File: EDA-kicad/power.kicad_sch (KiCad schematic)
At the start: 86 parts, among them Q4 NMOS, SW6 CHP-041B, U10 BAT-CONNECTOR-FLTS22WR00, U11 BQ25792RQMR, U2 TPS650250RHBR

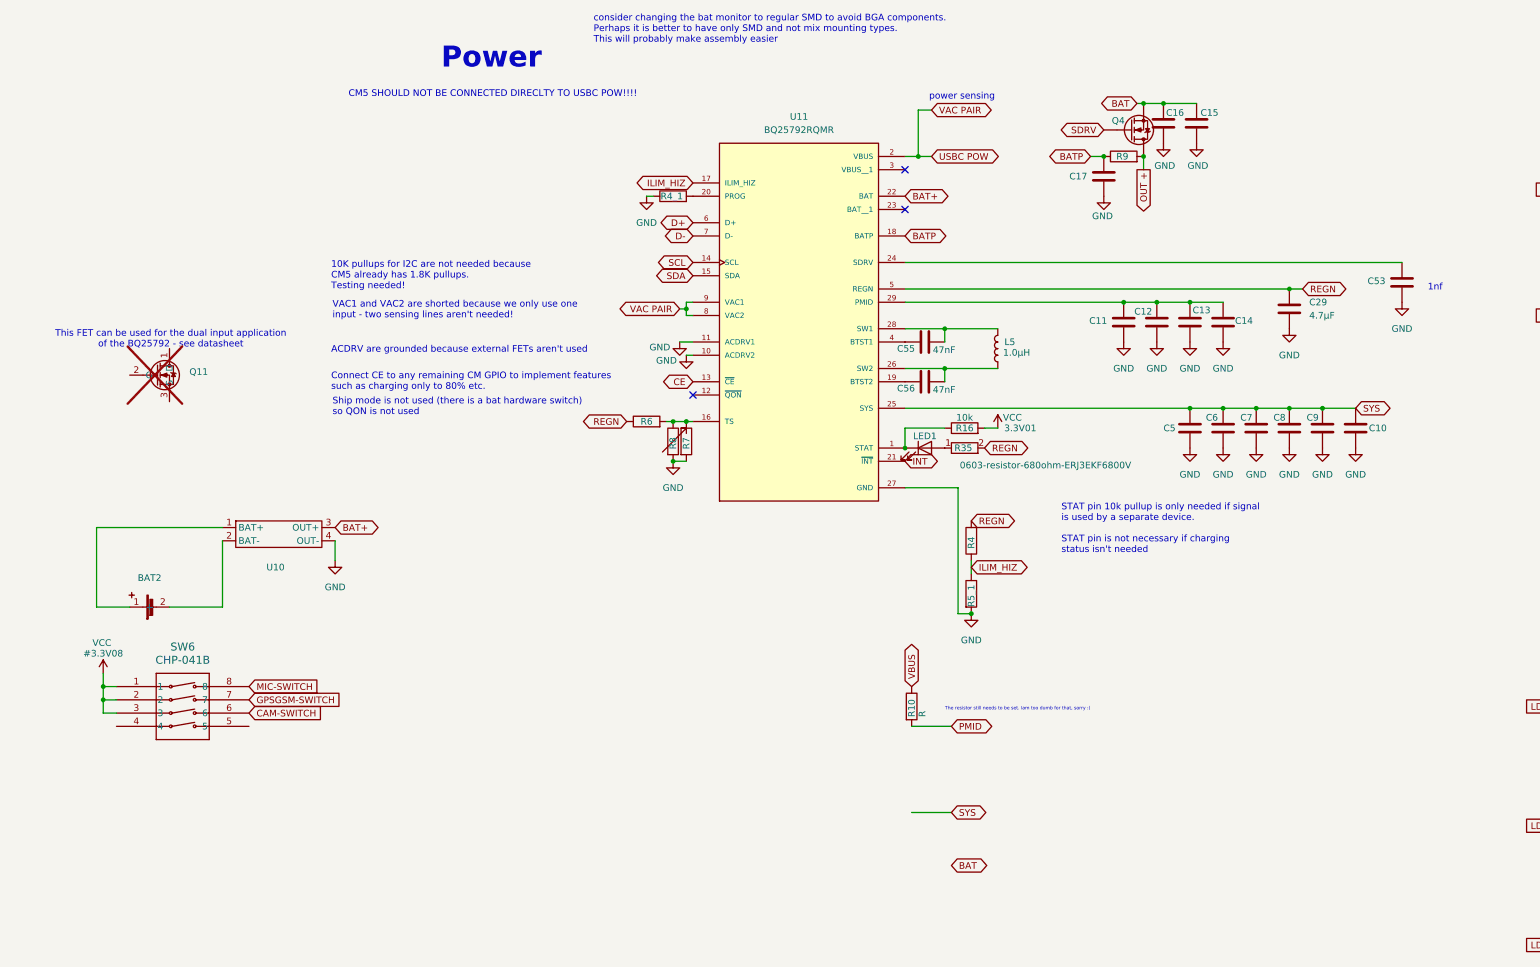
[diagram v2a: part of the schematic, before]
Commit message: connect charger IC pins 1 though 20
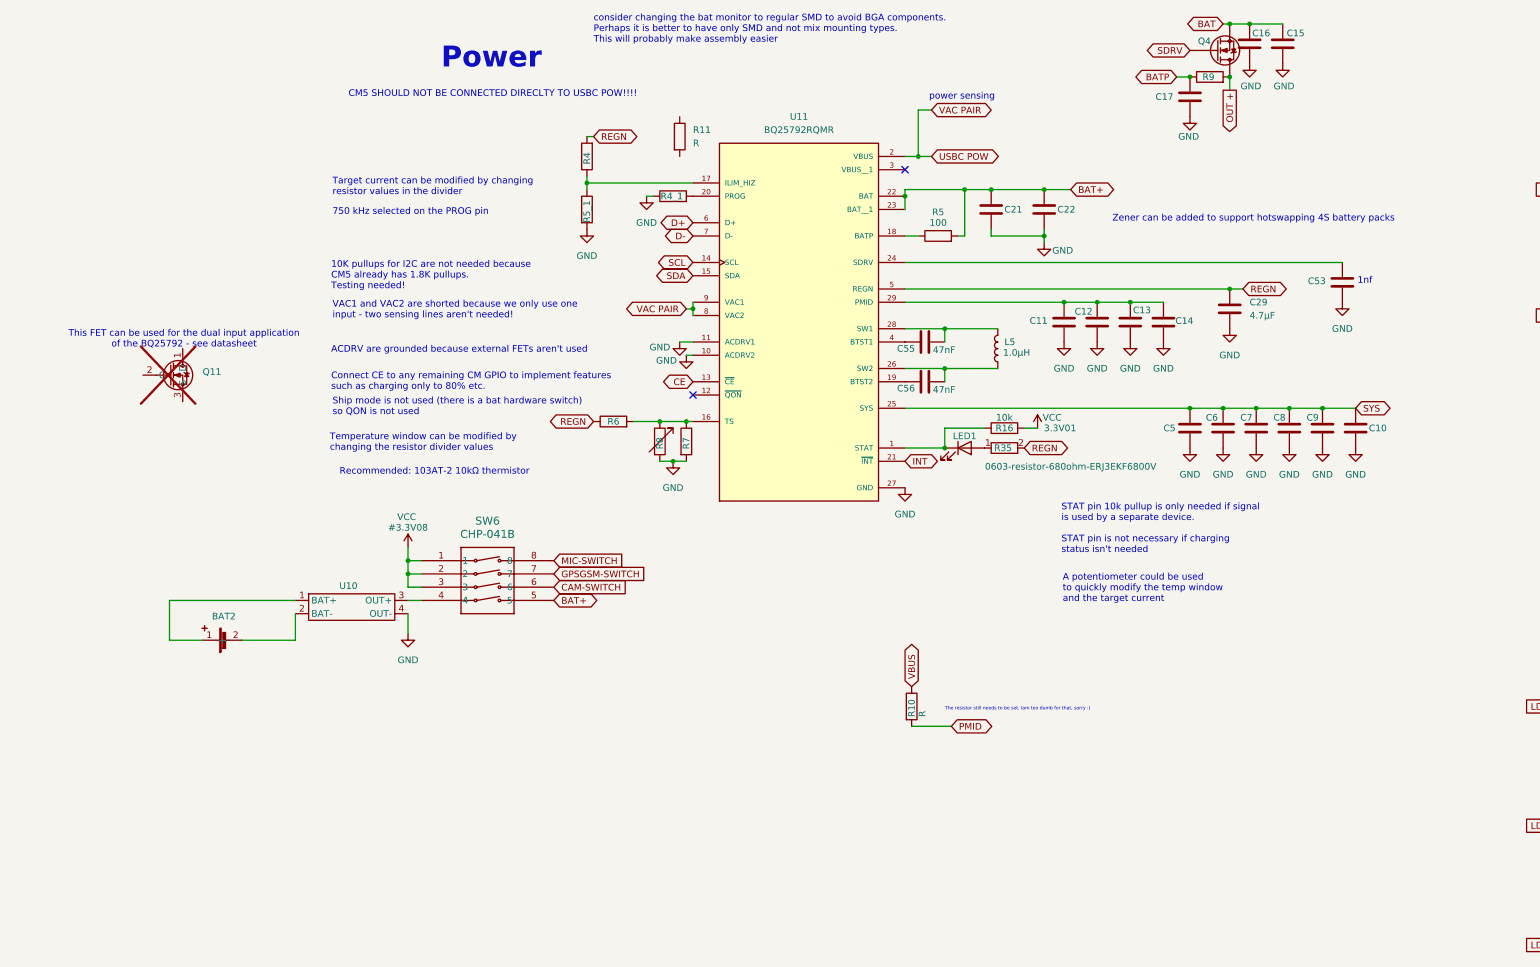
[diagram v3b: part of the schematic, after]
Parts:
- added C21, C22: 10μF, SPIRIT-footprints:USBC_capacitor_CAPC0603X33N, symbol Device:C
- added R11: R, symbol Device:R
- added R5: 100, symbol Device:R
- R4_1: value 6.04k -> 4.7K
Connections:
- net BAT+: now also SW6.5, U11.23 (BAT__1), C21.1, C22.1, R5.2; no longer U10.3 (OUT+)
- net BATP: no longer U11.18 (BATP)
- net GND: now also C21.2, C22.2
- net at SW6.4: now also U10.3 (OUT+)
- net ILIM_HIZ: no longer names the net of R4.1, R5_1.1, U11.17 (ILIM_HIZ)
- new net: R5.1, U11.18 (BATP)
- no-connect marks 4 -> 3
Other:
- note added: "750 kHz selected on the PROG pin"
- note added: "A potentiometer could be used to quickly modify the temp window and the target current"
- note added: "Recommended: 103AT-2 10kΩ thermistor"
- note added: "Target current can be modified by changing resistor values in the divider"
- note added: "Temperature window can be modified by changing the resistor divider values"
- note added: "Zener can be added to support hotswapping 4S battery packs"
- moved on the sheet: BAT2, C11, C12, C13, C14, C15, C16, C17, C29, C53, LED1, Q11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

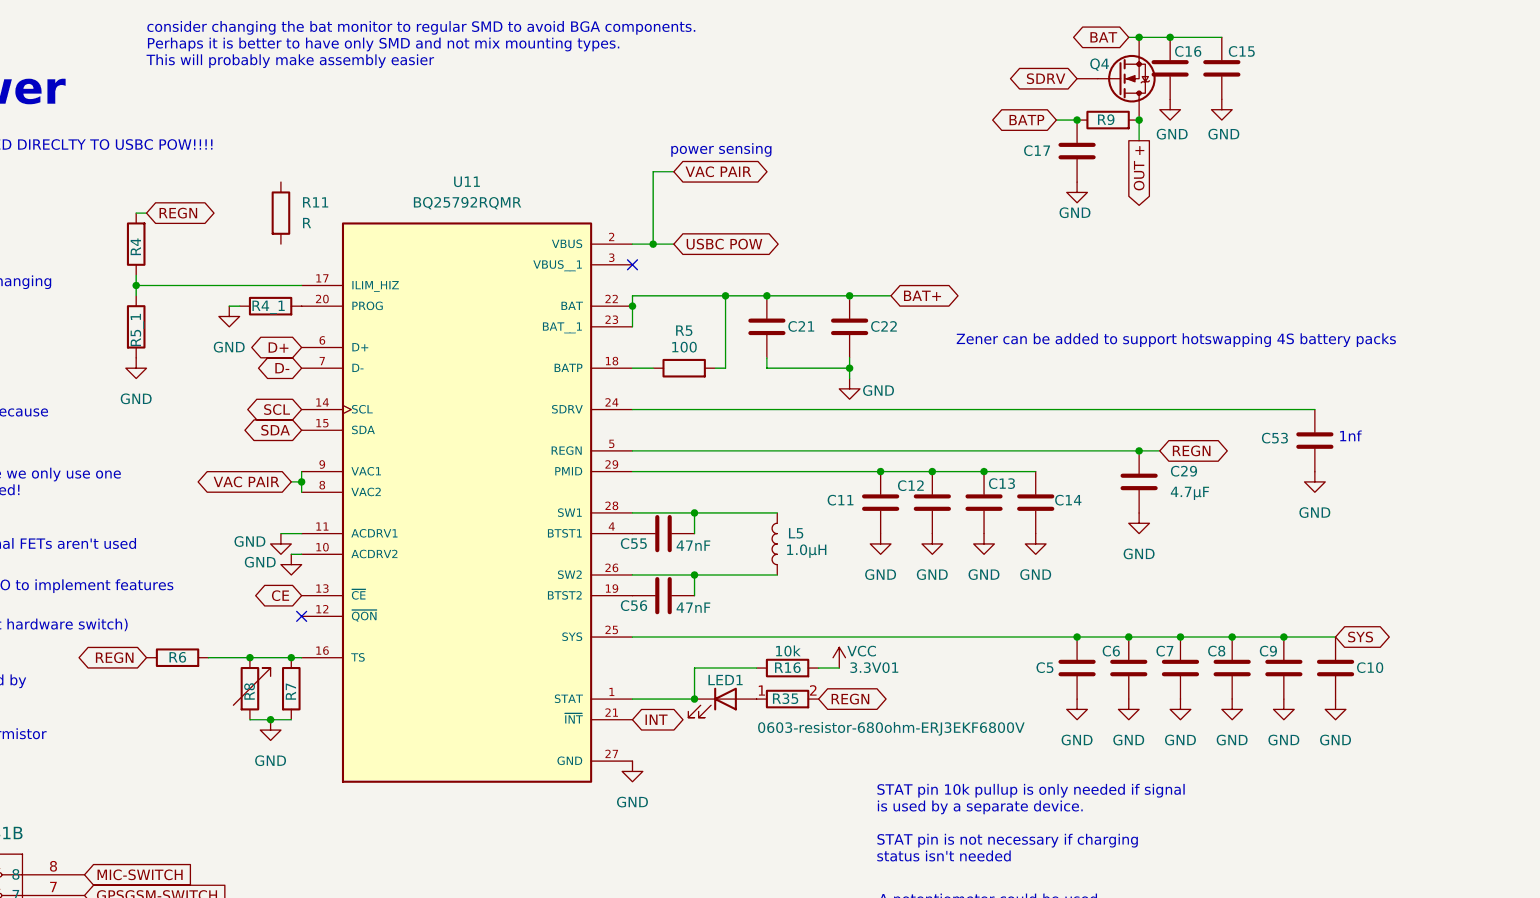
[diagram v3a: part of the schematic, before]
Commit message: exclude old EC25 and minor changes to power
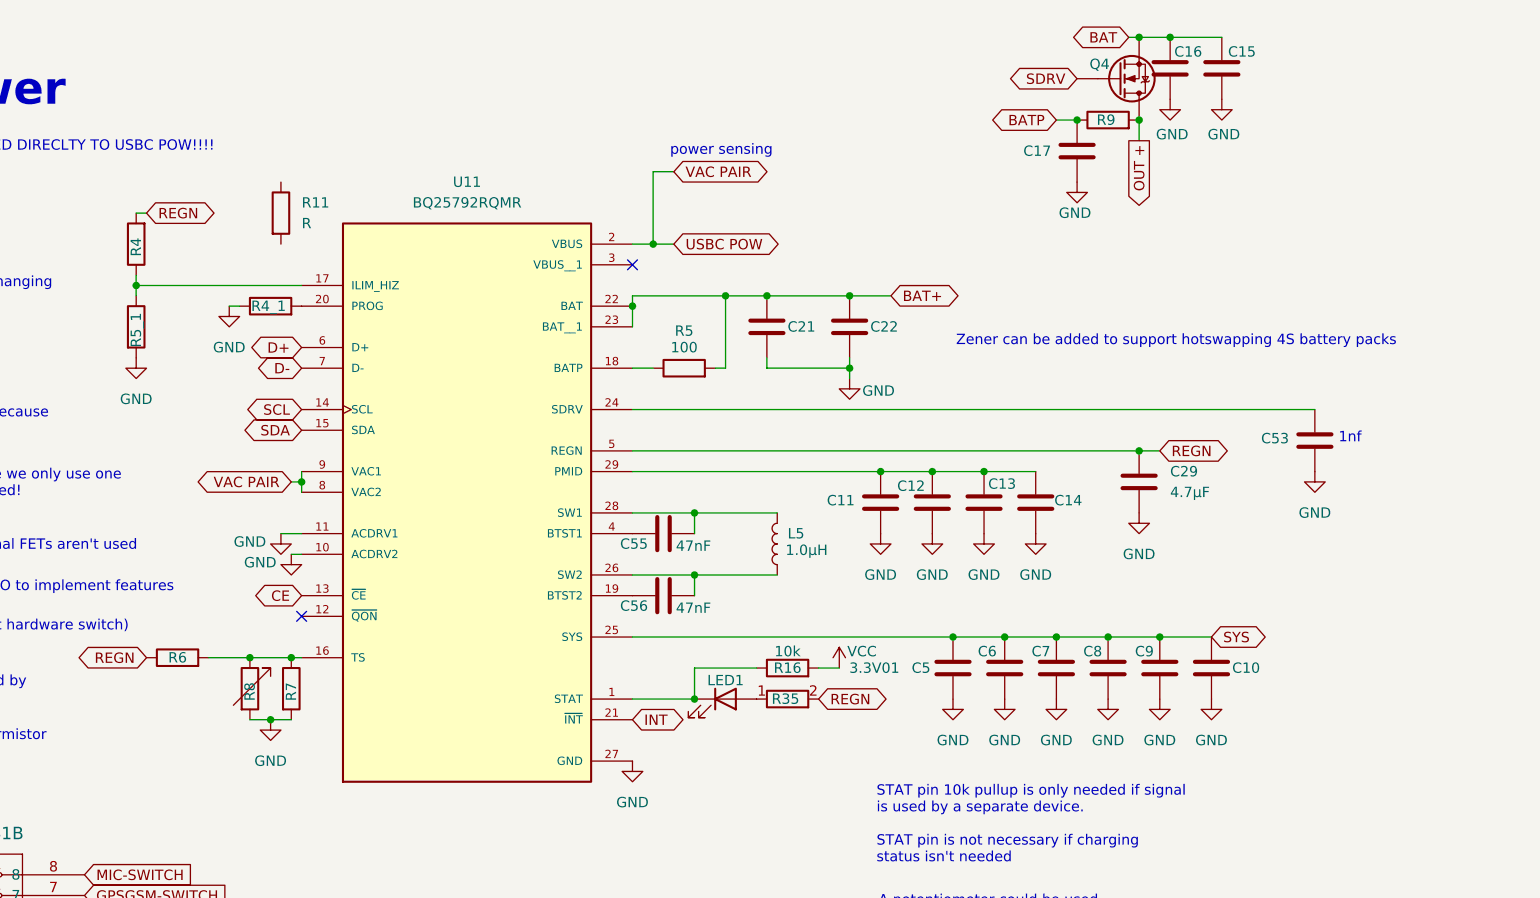
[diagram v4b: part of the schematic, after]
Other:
- note removed: "consider changing the bat monitor to regular SMD to avoid BGA components. Perhaps it is better to have only SMD and not mix mounting types. This will probably make assembly easier"
- moved on the sheet: C10, C5, C6, C7, C8, C9

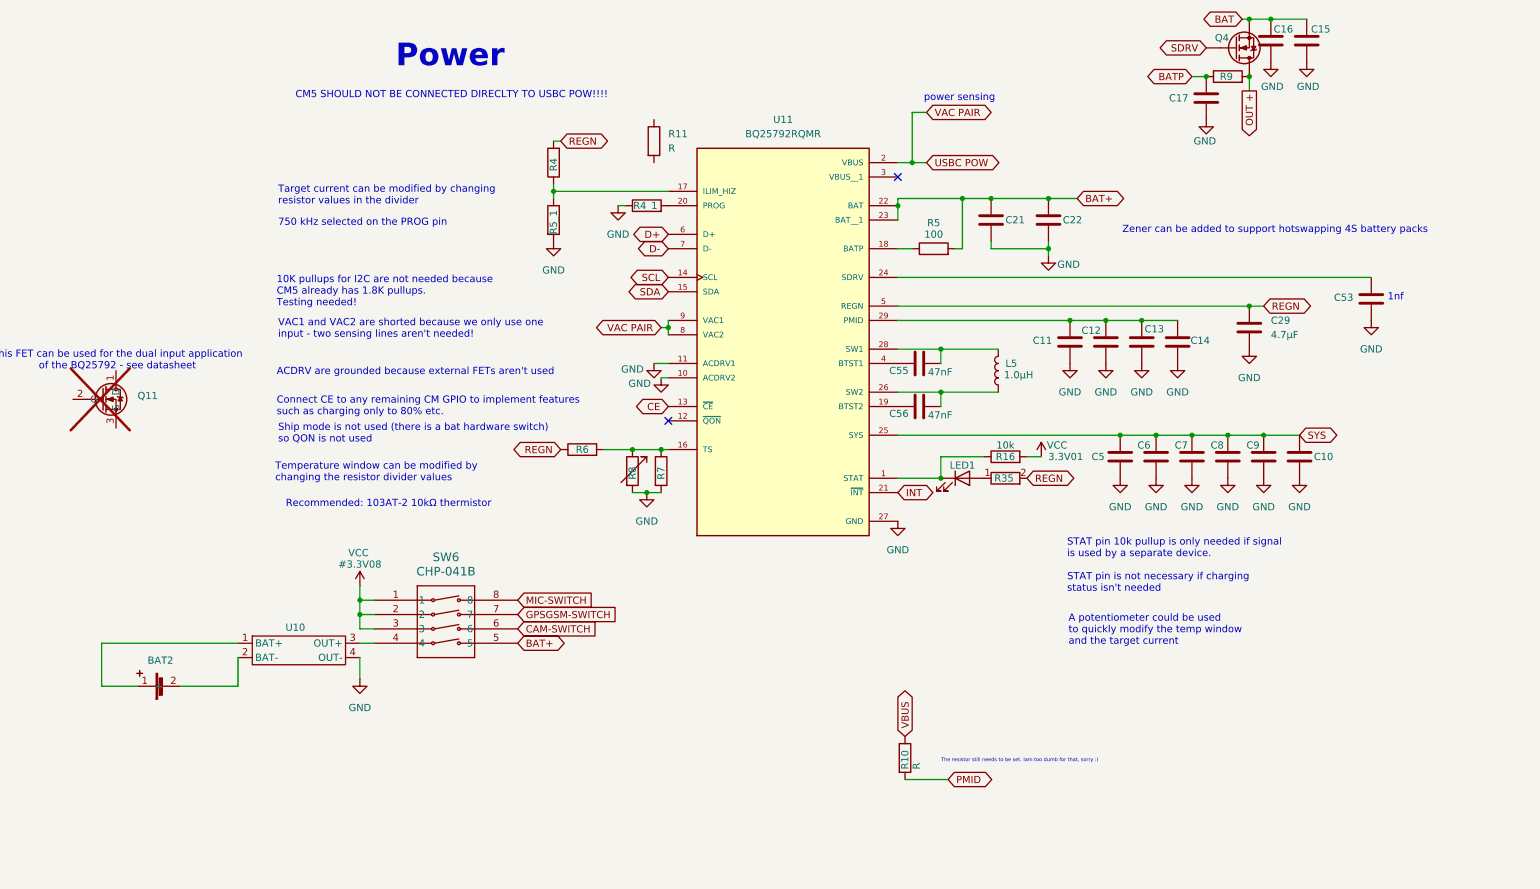
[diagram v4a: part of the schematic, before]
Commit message: charger IC fully connected
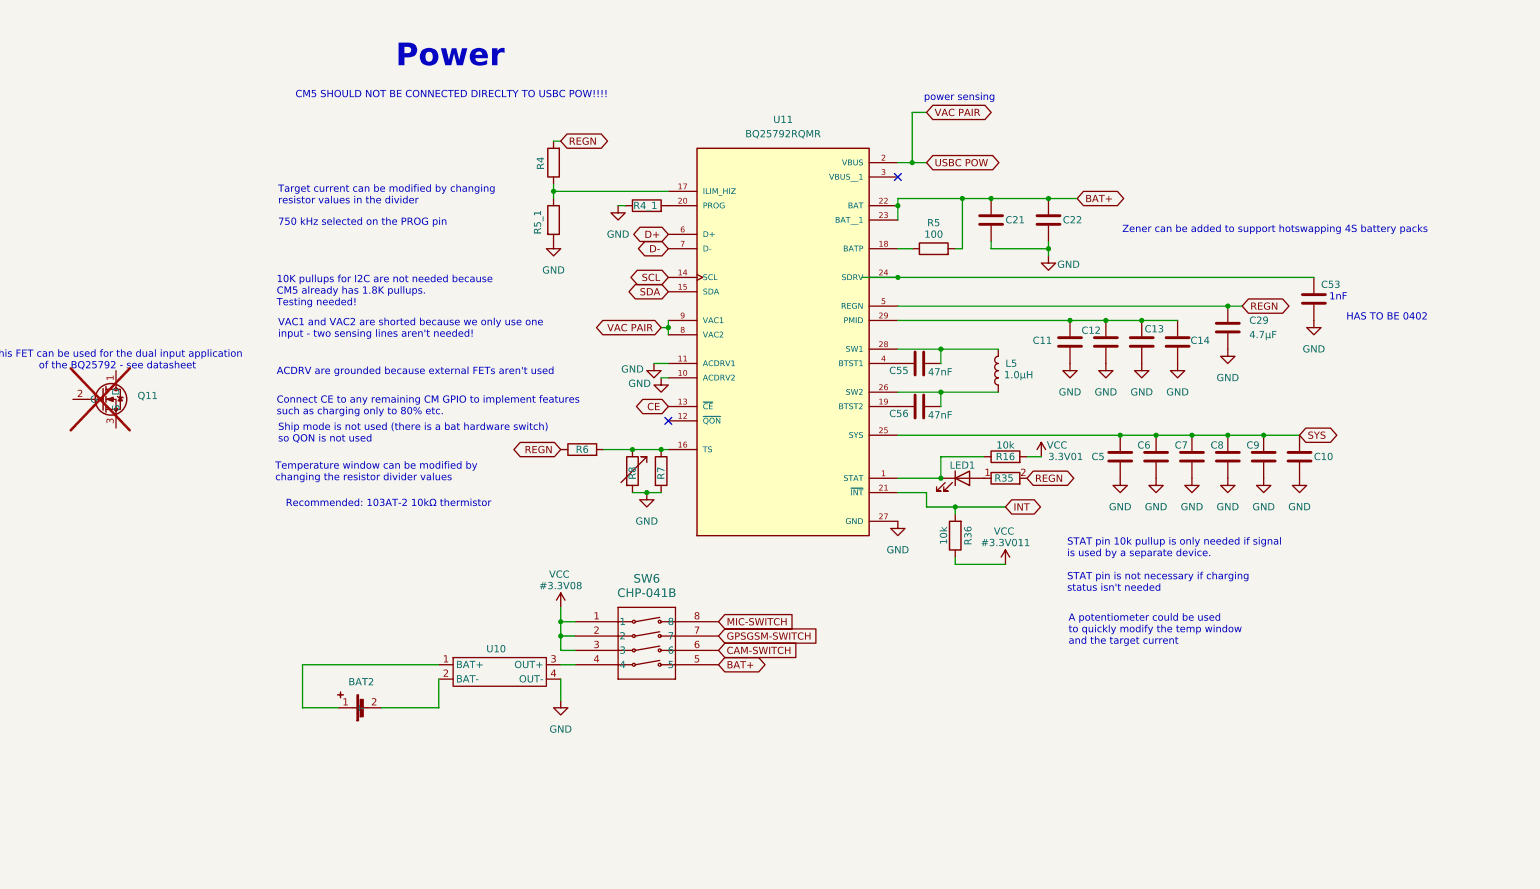
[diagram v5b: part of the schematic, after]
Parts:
- removed C15, C16: 10μF, SPIRIT-footprints:USBC_capacitor_CAPC0603X33N, symbol Device:C
- removed C17: 47nF, symbol Device:C
- removed Q4: NMOS, SPIRIT-footprints:gpio-driver-transistor-fix-SOT65P210X110-3N, symbol Simulation_SPICE:NMOS
- removed R10: R, SPIRIT-footprints:1K-05W-0805-RES_ERJP06J102V, symbol Device:R
- removed R11: R, symbol Device:R
- removed R9: 100, SPIRIT-footprints:1K-05W-0805-RES_ERJP06J102V, symbol Device:R
- added R36: 10k, symbol Device:R
- C53: value 0.1μF -> 1nF 50V
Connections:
- net INT: now also R36.2
- net VCC: now also R36.1
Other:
- note added: "1nF"
- note added: "HAS TO BE 0402"
- note removed: "1nf"
- note removed: "The resistor still needs to be set. Iam too dumb for that, sorry :("
- moved on the sheet: BAT2, C29, C53, SW6, U10

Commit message: power improvements
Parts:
- renumbered MP1 to MP3429GL-Z
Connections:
- net GND renamed AGND
- net MODE: no longer names the net of MP3429GL-Z.4 (MODE)
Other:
- note added: "CM 5A 5V"
- note added: "I think D variant should be chosen but not sure TODO ask Nima why he chose A? open a gh issue???"
- note added: "LCD 22V 700mA (?)"
- note added: "PSM mode selected"
- note added: "PWM signal to CE can change LCD brightness"
- note added: "Rails: 1x 22V 2x 5V 1x 3.3 1x 1.8"
- note added: "Switches + battery"
- moved on the sheet: BAT2, C10, C11, C12, C13, C14, C18, C19, C20, C21, C22, C29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
